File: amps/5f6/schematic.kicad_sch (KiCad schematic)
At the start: 69 parts, among them T3 2R sec

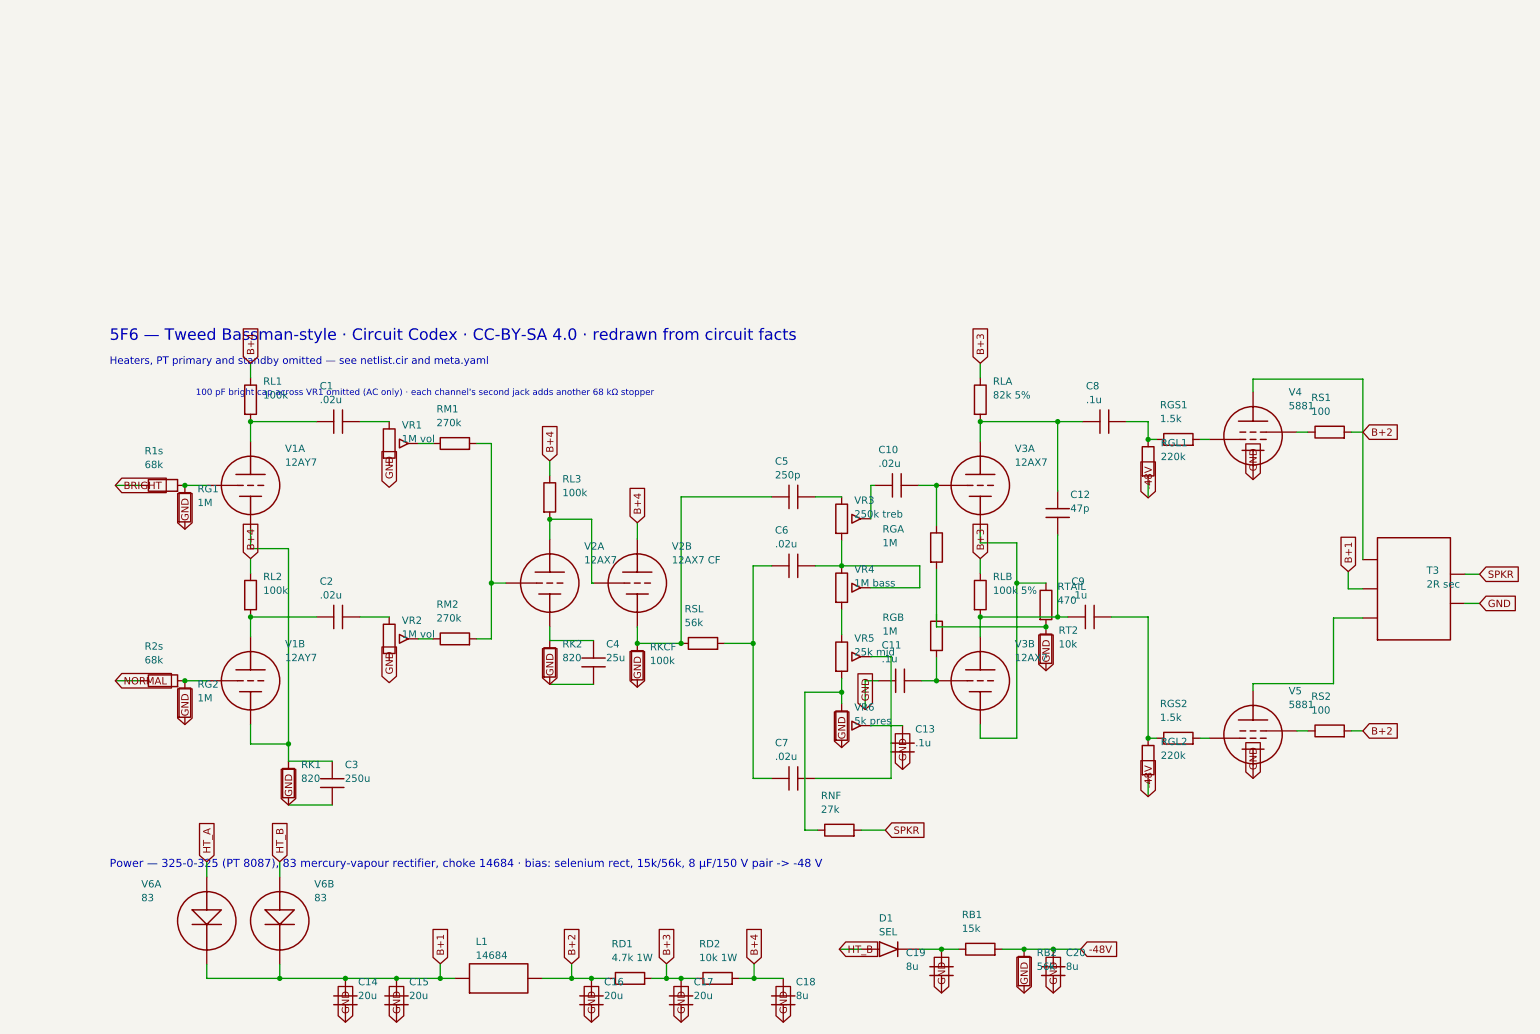
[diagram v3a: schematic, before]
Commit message: Update: regenerate every drawing the four merged units changed
The four parallel units all rewrote generators, so their committed artifacts
were each generated against only their own third of the merged pipeline. Every
schematic, both layout styles, the social cards and the manifest are rebuilt
here from the merged sources, so what ships is what the merged generators draw.

One integration fault the rebuild exposed, invisible to any single unit:

- 5E5-A: the note explaining that the Presence wiper and the 100k feedback
  resistor land on V3A's GRID (not its cathode, as on the 5F4) was added as a
  hand-placed `s.text()` at a coordinate chosen before the sheet gained a
  reserved notes band. Merged, it printed through the -32V bias label. Moved to
  `note()`, which wraps prose into that band — the exact failure mode the band
  was built to end.

Three conflicts resolved against docs/lettering-conventions.md rather than by
picking a side, since two units had corrected the same lines for different
reasons:

- 5E5-A tone/feedback caps take the corrected designators (C7, C8, C9, RNF —
  `C_tr1`/`C_NFB` were generator identifiers that had leaked onto a published
  board) with the house-derived lettering (`.01u 400V`, `500p`, `.1u 200V`).
  Dropping the working voltage or writing `.0005u` would have lost a rating the
  source prints and re-broken the pF/µF decade rule.
- 5D3 C6 and 6G6-B's three cathode resistors take the SI-prefix form the
  convention binds (`.005u`, `2.7k`, `1.5k`), keeping the ground-flag direction
  fix and the removal of the second `gnd()` that shorted each cathode it biased.
- 5F6-A's bias supply keeps both 8 µF cans drawn — the second was previously a
  parenthetical claiming one of two was shown — at the coordinates that clear
  the title-block strip.

All gates green, including check_value_consistency at zero disagreements.

🤖 Generated with [Claude Code](https://claude.com/claude-code)

Co-Authored-By: Claude Fable 5 <noreply@anthropic.com>
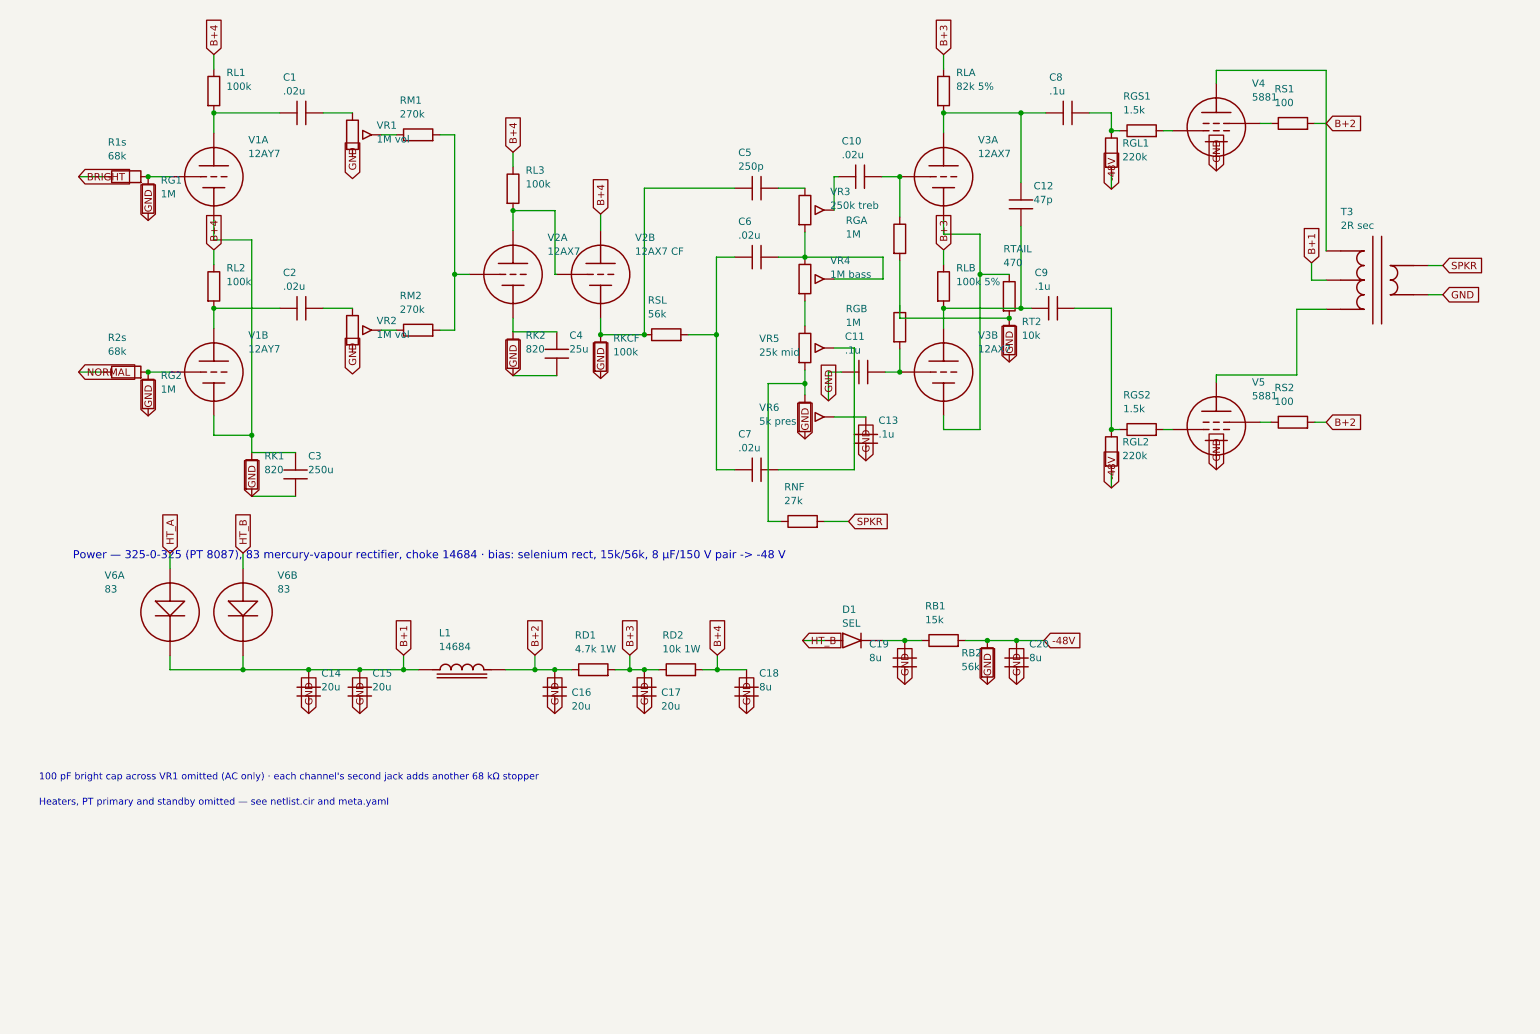
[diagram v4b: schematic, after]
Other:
- note removed: "5F6 — Tweed Bassman-style · Circuit Codex · CC-BY-SA 4.0 · redrawn from circuit facts"
- company: (none) -> Circuit Codex
- title: (none) -> 5F6 — Tweed Bassman-style

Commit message: Fix: rotated global labels lettered their net names outside the flag
Every global label this pipeline emitted carried (justify left) regardless of
rotation. KiCanvas — like KiCad — draws label text horizontally at 0/180 and
vertically at 90/270 and reads WHICH SIDE of the anchor it letters on from the
justification, so at 180 and 270 the name printed outside an empty flag
outline, struck through by the very wire it names: 219 labels at 180 deg
(including the input-jack flags at top-left of nearly every sheet, the first
glyphs a visitor reads) and 792 GND/rail flags at 270 whose names squeezed at
the flag mouth instead of lettering down the body. The library already
compensated rotation for property text (`pa`); this mirrors that logic for
global labels: justify right at 180/270, left at 0/90.

check_schematics gains the geometry clause whose absence let all 1011
instances through a "no lettering through circuitry" pass: it modelled the
flag box but never the label TEXT, so a name rendered on the wrong side was
invisible to it. The gate now proves justification compensates rotation on
every global label.

Two more things this exposed, fixed in the same engine pass:

- Placement now measures with the renderer's own Newstroke advance table
  (extracted from the vendored kicanvas.js) instead of a flat 0.68-em prose
  average that under-read part lettering by a quarter — the mechanism behind
  every "metered clean, printed through its neighbour" incident. The GATE
  deliberately keeps the coarse ruler: re-ruling it with renderer truth was
  tried and red-flagged 28 of 34 sheets over abutments three visual passes
  had already judged sub-visual (the two-rulers note in schematic_lib.py).
- place_captions' escape ladder runs further, because a banner caption
  measured truly is half again wider than the old estimate believed.

All 34 schematics regenerated; full gate suite green.

🤖 Generated with [Claude Code](https://claude.com/claude-code)

Co-Authored-By: Claude Fable 5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
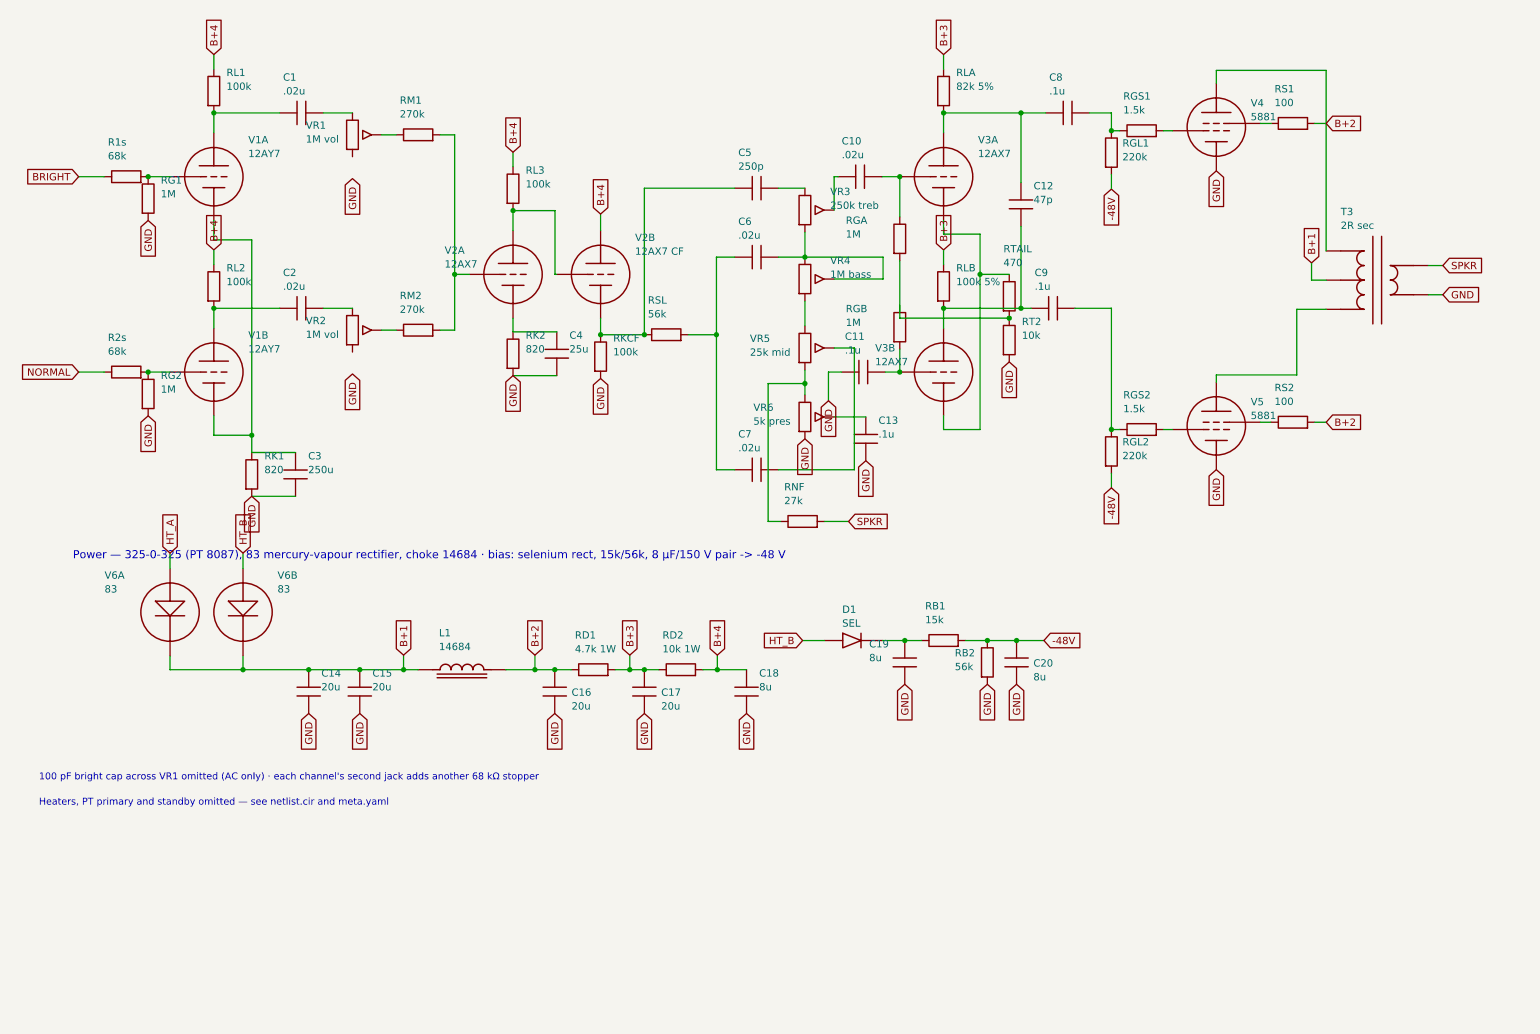
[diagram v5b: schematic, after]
